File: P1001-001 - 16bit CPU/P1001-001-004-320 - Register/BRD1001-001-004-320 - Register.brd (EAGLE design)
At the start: 200 x 48 mm, 20 parts, among them IC1 74HC173D, IC12 74AC245DW, IC2 74HC173D, IC27 MEGA8535-A, IC3 74HC173D, IC4 74HC173D, IC7 74AC245DW, J1 22-27-2041-04, J3 22-27-2041-04, J4 22-27-2061-06

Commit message: Check in the first try at soldering up the board
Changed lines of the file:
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@@
 <text x="166" y="8" size="2.1844" layer="28" rot="MR0">P1001-001-004-320 - Register</text>
 <text x="164" y="4" size="2.1844" layer="28" rot="MR0">Copyright 2020 James Wright</text>
+<hole x="4" y="44" drill="3"/>
+<hole x="4" y="4" drill="3"/>
+<hole x="196" y="4" drill="3"/>
+<hole x="196" y="44" drill="3"/>
 </plain>
 <attributes>

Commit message: ALU Register and controllker layout
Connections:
- net BUS3: no longer IC12.6
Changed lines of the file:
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@@
 <signal name="BUS3">
 <contactref element="IC3" pad="14"/>
-<contactref element="IC12" pad="6"/>
 <contactref element="BACKBUS" pad="4"/>
 <contactref element="FRONTBUS" pad="4"/>
 <wire x1="7.239" y1="31.3182" x2="21.9456" y2="31.3182" width="0.1524" layer="1"/>
 <wire x1="6.3246" y1="30.4038" x2="7.239" y2="31.3182" width="0.1524" layer="1"/>
-<wire x1="21.9456" y1="31.3182" x2="21.9708" y2="31.365" width="0.1524" layer="1"/>
 <wire x1="6.3246" y1="30.4038" x2="6.27" y2="30.35" width="0.1524" layer="1"/>
 <wire x1="36.6522" y1="15.5448" x2="40.9194" y2="15.5448" width="0.1524" layer="16"/>
@@
 <wire x1="22.0218" y1="31.3944" x2="22.4028" y2="31.3944" width="0.1524" layer="1"/>
 <wire x1="196.215" y1="30.4038" x2="196.27" y2="30.35" width="0.1524" layer="16"/>
-<wire x1="22.0218" y1="31.3944" x2="21.9708" y2="31.365" width="0.1524" layer="1"/>
 <via x="24.3078" y="33.2994" extent="1-16" drill="0.35"/>
+<wire x1="21.9456" y1="31.3182" x2="22.0218" y2="31.3944" width="0" layer="19" extent="1-1"/>
 </signal>
 <signal name="BUS8">

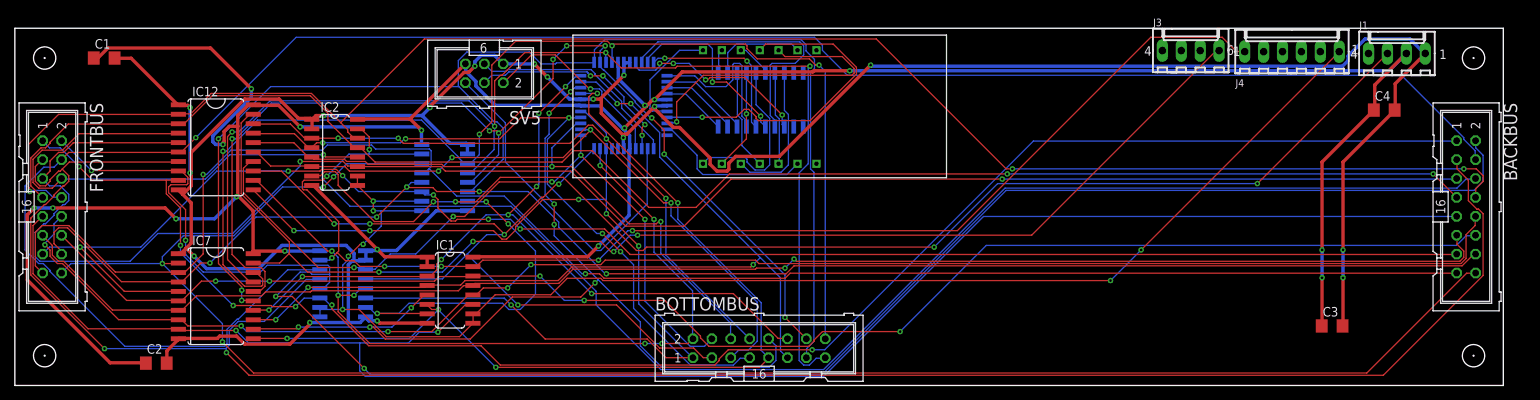
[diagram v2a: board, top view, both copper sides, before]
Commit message: add ram to Memory
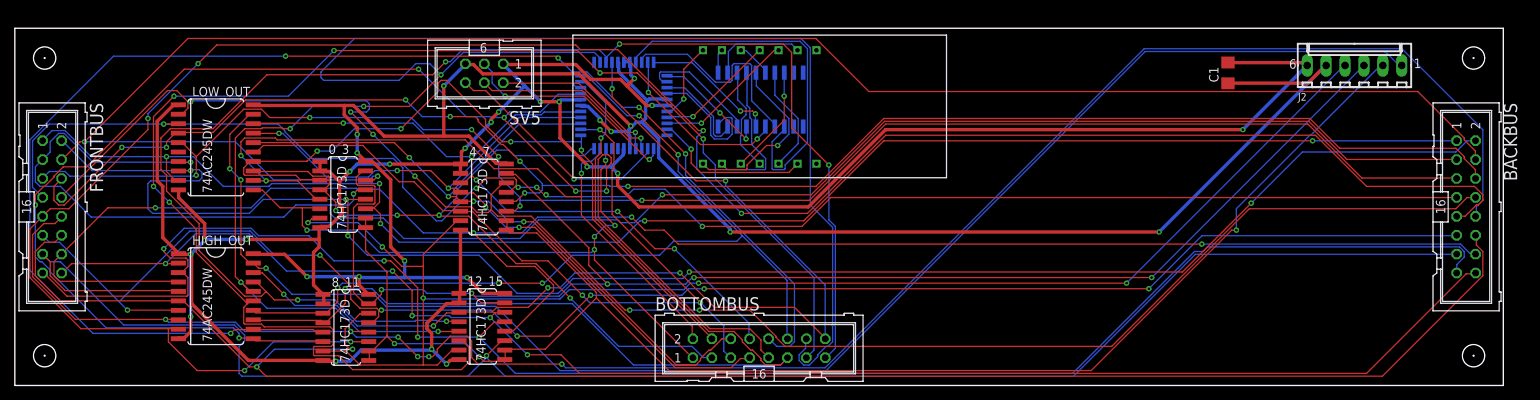
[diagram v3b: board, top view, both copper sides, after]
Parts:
- removed C2, C3, C4: 1uF, rcl:C1206
- removed IC1, IC2, IC3, IC4: 74HC173D, 74xx-eu:SO16
- removed J1, J3: 22-27-2041-04, con-molex:6410-04
- removed J4: 22-27-2061-06, con-molex:6410-06
- added 0_3, 12_15, 4_7, 8_11: 74HC173D, 74xx-eu:SO16
- added J2: 22-27-2061-06, con-molex:6410-06
- moved C1 151.0 mm to (163.0, 42.0), turned to 90 degrees
- renumbered IC12 to LOW_OUT, IC7 to HIGH_OUT
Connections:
- net !REG_IN: now also 0_3.10, 0_3.9, 12_15.10, 12_15.9, 4_7.10, 4_7.9, 8_11.10, 8_11.9, J2.2; no longer IC1.10, IC1.9, IC2.10, IC2.9, IC3.10, IC3.9, IC4.10, IC4.9, J4.1
- net !REG_OUT: now also J2.1; no longer J3.1
- net BUS0: now also 0_3.11; no longer IC3.11
- net BUS1: now also 0_3.12; no longer IC3.12
- net BUS10: now also 8_11.13; no longer IC1.13
- net BUS11: now also 8_11.14; no longer IC1.14
- net BUS12: now also 12_15.11; no longer IC4.11
- net BUS13: now also 12_15.12; no longer IC4.12
- net BUS14: now also 12_15.13; no longer IC4.13
- net BUS15: now also 12_15.14; no longer IC4.14
- net BUS2: now also 0_3.13; no longer IC3.13
- net BUS3: now also 0_3.14; no longer IC3.14
- net BUS4: now also 4_7.11; no longer IC2.11
- net BUS5: now also 4_7.12; no longer IC2.12
- net BUS6: now also 4_7.13; no longer IC2.13
- net BUS7: now also 4_7.14; no longer IC2.14
- net BUS8: now also 8_11.11; no longer IC1.11
- net BUS9: now also 8_11.12; no longer IC1.12
- net CLEAR: now also 0_3.15, 12_15.15, 4_7.15, 8_11.15, J2.3; no longer IC1.15, IC2.15, IC3.15, IC4.15, J4.6
- net CLK: now also 0_3.7, 12_15.7, 4_7.7, 8_11.7, J2.4; no longer IC1.7, IC2.7, IC3.7, IC4.7, J1.3
- net GND: now also 0_3.1, 0_3.2, 0_3.8, 12_15.1, 12_15.2, 12_15.8, 4_7.1, 4_7.2, 4_7.8, 8_11.1, 8_11.2, 8_11.8, J2.6; no longer C2.2, C3.2, C4.2, IC1.1, IC1.2, IC1.8, IC2.1, IC2.2, IC2.8, IC3.1, IC3.2, IC3.8, IC4.1, IC4.2, IC4.8, J1.1
- net SIGNAL0: now also 0_3.6; no longer IC3.6
- net SIGNAL1: now also 0_3.5; no longer IC3.5
- net SIGNAL10: now also 8_11.4; no longer IC1.4
- net SIGNAL11: now also 8_11.3; no longer IC1.3
- net SIGNAL12: now also 12_15.6; no longer IC4.6
- net SIGNAL13: now also 12_15.5; no longer IC4.5
- net SIGNAL14: now also 12_15.4; no longer IC4.4
- net SIGNAL15: now also 12_15.3; no longer IC4.3
- net SIGNAL2: now also 0_3.4; no longer IC3.4
- net SIGNAL3: now also 0_3.3; no longer IC3.3
- net SIGNAL4: now also 4_7.6; no longer IC2.6
- net SIGNAL5: now also 4_7.5; no longer IC2.5
- net SIGNAL6: now also 4_7.4; no longer IC2.4
- net SIGNAL7: now also 4_7.3; no longer IC2.3
- net SIGNAL8: now also 8_11.6; no longer IC1.6
- net SIGNAL9: now also 8_11.5; no longer IC1.5
- net VCC: now also 0_3.16, 12_15.16, 4_7.16, 8_11.16, J2.5; no longer C2.1, C3.1, C4.1, IC1.16, IC2.16, IC3.16, IC4.16, J1.2
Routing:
- net VCC: track 396.4 -> 289.0 mm, vias 16 -> 12
- net SIGNAL13: track 144.9 -> 245.7 mm, vias 9 -> 5
- net SIGNAL8: track 125.2 -> 200.9 mm, vias 5 -> 6
- net SIGNAL9: track 125.5 -> 197.4 mm, vias 8 -> 5
- net BUS8: track 233.8 -> 294.4 mm, vias 2 -> 6
- net GND: track 409.6 -> 360.5 mm, vias 18 -> 19
- net SIGNAL0: track 132.9 -> 89.8 mm, vias 6 -> 5
- net BUS2: track 282.6 -> 240.1 mm, vias 2 -> 3
- net BUS9: track 211.7 -> 252.9 mm, vias 5 -> 6
- net BUS15: track 246.8 -> 211.5 mm, vias 4 -> 5
- net BUS11: track 205.4 -> 240.6 mm, vias 5 -> 2
- net !REG_OUT: track 167.2 -> 202.0 mm, vias 4 -> 3
- net BUS13: track 211.6 -> 242.7 mm, vias 5 -> 4
- net SIGNAL14: track 165.2 -> 195.8 mm, vias 4 -> 5
- net BUS5: track 250.7 -> 220.1 mm, vias 1 -> 7
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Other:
- board text added: "P1001-001-004-320 A Register"
- board text removed: "P1001-001-004-320 - Register"
